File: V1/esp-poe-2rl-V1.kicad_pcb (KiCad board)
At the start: 2 copper layers, 89 x 45 mm, 90 parts, among them J1 USB_C_Receptacle_USB2.0, J2 RJ45 JACK, J3 1x2P 5,08mm, J4 1x2P 5,08mm, K1 G5NB-1A-E-DC5, K2 G5NB-1A-E-DC5, Q1 UMH3N, Q2 WPM2015-3/TR, Q3 LMUN2211LT1G, Q4 MMBT2222A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

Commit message: Update image
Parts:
- J3, J4: footprint Tales:TerminalBlock_Dibo_DB142R-2-5.08_1x02_P5.08mm_Horizontal -> Tales:TerminalBlock_Dibo_DB142R-5.08-2P_1x02_P5.08mm_Horizontal
- L2: footprint Tales:L_3x3_h1.5 -> Tales:L_3x3mm_h1.5mm

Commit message: Added temperature sensor
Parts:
- added C26: 100nF/50V, Tales:C_0402_1005Metric, F.Cu at (124.4, 60.1)
- added R31: 2k2/62,5mW, Tales:R_0402_1005Metric, F.Cu at (121.5, 60.1)
- added R32: 2k2/62,5mW, Tales:R_0402_1005Metric, F.Cu at (121.5, 62.1)
- added U7: AHT20, Tales:DFN-6-3x3mm_P1mm, F.Cu at (117.4, 61.5)
- D10, D9: footprint Tales:D_SOD-123 -> Diode_THT:D_DO-35_SOD27_P7.62mm_Horizontal
- Q1: footprint Tales:SOT-363_SC-70-6 -> Package_TO_SOT_SMD:SOT-363_SC-70-6
- U2: footprint Tales:SOIC-8-1EP_3.9x4.9mm_P1.27mm_EP2.29x3mm_ThermalVias -> Tales:SOIC-8-1EP_3.9x4.9mm_P1.27mm_EP2.41x3.81mm_ThermalVias
- U4: footprint Tales:SOIC-16_3.9x9.9mm_P1.27mm -> Package_SO:SOIC-16_3.9x9.9mm_P1.27mm
- U5: footprint Tales:ESP32-WROOM-32U -> RF_Module:ESP32-WROOM-32U
- U6: footprint Tales:QFN-32-1EP_5x5mm_P0.5mm_EP3.3x3.3mm_ThermalVias -> Package_DFN_QFN:QFN-32-1EP_5x5mm_P0.5mm_EP3.3x3.3mm_ThermalVias
- moved K1 0.23 mm to (83.8, 80.6)
- moved K2 0.21 mm to (97.2, 80.6)
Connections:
- U5 pad 16: unconnected-(U5-IO13-Pad16) -> OUT1
- U5 pad 27: unconnected-(U5-IO16-Pad27) -> OUT2
- U5 pad 8: OUT2 -> I2C_SCL
- U5 pad 9: OUT1 -> I2C_SDA
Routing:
- net OUT1: track 20.0 -> 1.50 mm
- net OUT2: track 8.27 -> 1.50 mm

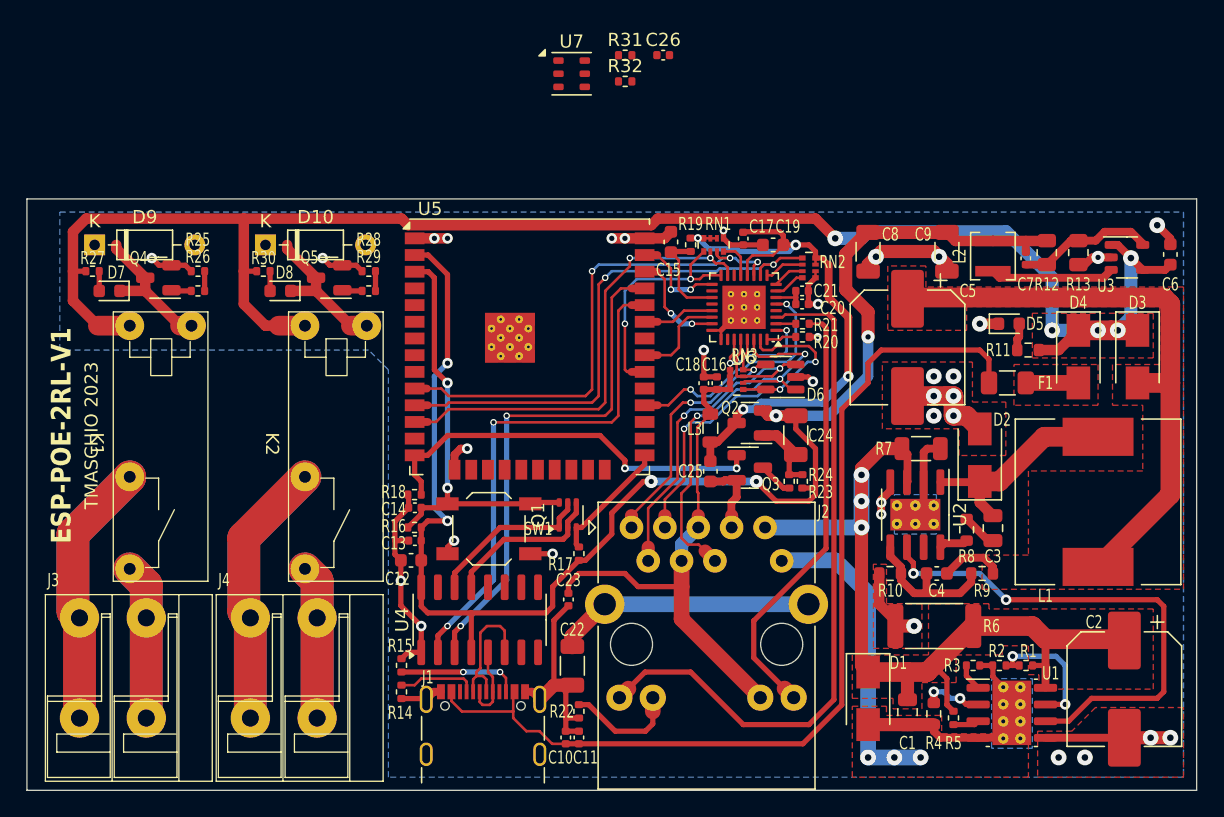
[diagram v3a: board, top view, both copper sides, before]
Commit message: Added temperature sensor.
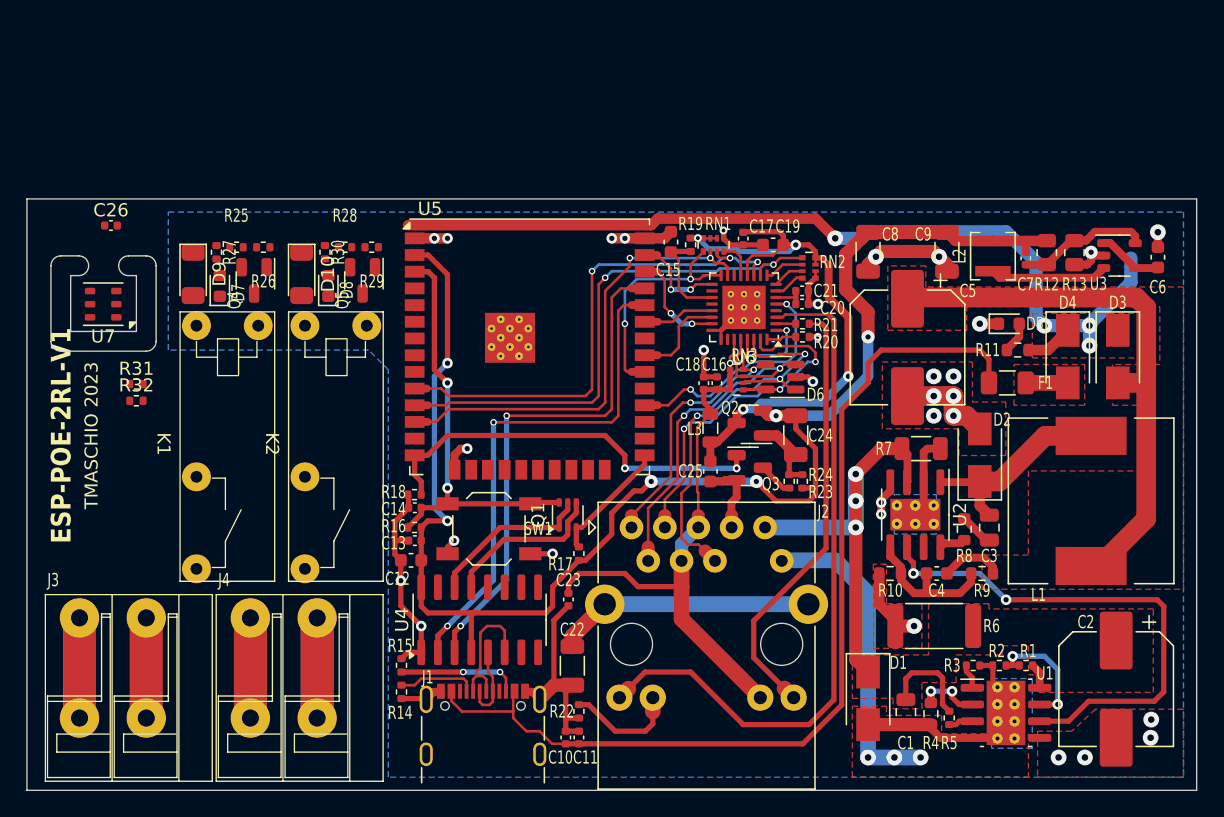
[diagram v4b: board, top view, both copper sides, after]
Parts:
- D10, D9: footprint Diode_THT:D_DO-35_SOD27_P7.62mm_Horizontal -> Tales:D_SOD-123
- moved R31 44.8 mm to (84.3, 85.1)
- moved R32 44.4 mm to (84.3, 86.4)
- moved C26 44.0 mm to (82.4, 73.0)
- moved U7 39.7 mm to (81.8, 79.0), turned to 180 degrees
- moved R27 9.54 mm to (90.4, 75.1), turned to -90 degrees
- moved D7 8.40 mm to (90.7, 77.6), turned to 90 degrees
- moved D9 7.81 mm to (88.6, 76.7), turned to -90 degrees
- moved Q4 7.29 mm to (93.3, 77.2), turned to -90 degrees
- moved R26 5.98 mm to (94.0, 74.7), turned to 180 degrees
- moved K1 5.08 mm to (88.9, 80.6)
- moved R30 4.91 mm to (98.7, 75.1), turned to -90 degrees
- moved D8 3.66 mm to (98.9, 77.6), turned to 90 degrees
- moved D10 3.53 mm to (96.9, 76.7), turned to -90 degrees
- moved R25 3.46 mm to (92.0, 74.7)
- moved R29 3.33 mm to (102.2, 74.7), turned to 180 degrees
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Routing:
- net +5V: track 130.2 -> 74.8 mm, vias 5 -> 4
- net Net-(J4-Pin_1): track 41.0 -> 15.2 mm
- net Net-(J3-Pin_1): track 40.7 -> 15.2 mm
- net PoE+: track 65.6 -> 42.9 mm
- net GND: track 113.2 -> 97.1 mm, vias 34 -> 32
- net Net-(D10-A): track 11.3 -> 0.00 mm
- net Net-(D7-K): track 11.0 -> 0.00 mm
- net Net-(J3-Pin_2): track 23.8 -> 15.2 mm
- net Net-(J4-Pin_2): track 23.5 -> 15.2 mm
- net 5VPOE: track 49.7 -> 47.1 mm
- net OUT2: track 1.50 -> 0.00 mm
- net OUT1: track 1.50 -> 0.00 mm
- net Net-(D8-A): track 1.50 -> 0.00 mm
- net Net-(D7-A): track 1.50 -> 0.00 mm
- net Net-(Q5-B): track 1.45 -> 0.00 mm
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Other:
- outline, holes or cut-outs redrawn

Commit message: Reviewing board for fabrication
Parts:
- U3: footprint Tales:TSOT-23-5 -> Tales:SOT-23-5_Shorter_Pins
- U5: footprint RF_Module:ESP32-WROOM-32U -> Tales:ESP32-WROOM-32U
- U6: footprint Package_DFN_QFN:QFN-32-1EP_5x5mm_P0.5mm_EP3.3x3.3mm_ThermalVias -> Tales:QFN-32-1EP_5x5mm_P0.5mm_EP3.3x3.3mm_ThermalVias
- moved RN1 0.21 mm to (128.3, 74.3)
- moved C19 0.20 mm to (132.8, 74.3)
- moved C20 0.15 mm to (135.1, 79.0)
- moved C21 0.15 mm to (135.1, 78.0)
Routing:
- net +5V: track 74.8 -> 113.5 mm, vias 4 -> 5
- net GND: track 97.1 -> 103.3 mm, vias 32 -> 34
- net Net-(D7-K): track 0.00 -> 5.27 mm
- net Net-(D10-A): track 0.00 -> 5.27 mm
- net +3.3VLAN: track 46.6 -> 49.5 mm
- net Net-(Q4-B): track 0.00 -> 1.63 mm
- net Net-(Q5-B): track 0.00 -> 1.63 mm
- net Net-(U4-RXD): track 39.1 -> 37.7 mm
- net Net-(D8-A): track 0.00 -> 1.38 mm
- net Net-(D7-A): track 0.00 -> 1.37 mm
- net /EMAC_MDC: track 7.32 -> 8.59 mm
- net OUT1: track 0.00 -> 1.01 mm
- net OUT2: track 0.00 -> 1.01 mm
- net /EMAC_MDIO: track 17.9 -> 18.7 mm
- net /EMAC_CLK: track 18.4 -> 17.6 mm
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
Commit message: Update esp-poe-2rl-V1.kicad_pcb
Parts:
- moved C7 1.55 mm to (151.6, 74.0)
- moved U3 0.83 mm to (159.2, 74.5)
- moved R13 0.82 mm to (155.2, 74.4), turned to 90 degrees
- moved L2 0.78 mm to (149.1, 74.7)
- moved R12 0.78 mm to (153.2, 74.4)
- moved C6 0.24 mm to (162.1, 75.2)
- moved C8 0.08 mm to (140.1, 75.0)
- moved C9 0.08 mm to (145.9, 75.0)
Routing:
- net 5VPOE: track 47.1 -> 5.39 mm
- net Net-(J3-Pin_1): track 15.2 -> 48.6 mm
- net Net-(J4-Pin_1): track 15.2 -> 42.5 mm
- net +3.3V: track 117.1 -> 93.2 mm
- net Net-(J3-Pin_2): track 15.2 -> 28.2 mm
- net GND: track 103.3 -> 90.9 mm, vias 34 -> 33
- net Net-(U3-FB): track 9.93 -> 0.00 mm
- net Net-(U3-LX): track 8.94 -> 0.00 mm
- net Net-(J4-Pin_2): track 15.2 -> 23.5 mm
- net +5V: track 113.5 -> 107.1 mm, vias 5 -> 4
- net /TD-: track 29.2 -> 25.8 mm
- net Net-(D10-A): track 5.27 -> 7.32 mm
- net Net-(D7-K): track 5.27 -> 7.32 mm
- net Net-(U4-TXD): track 38.6 -> 37.5 mm
- removed copper zone on B.Cu, net GND

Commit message: Update esp-poe-2rl-V1.kicad_pcb
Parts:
- moved C6 0.55 mm to (161.5, 75.2)
- moved U3 0.49 mm to (158.7, 74.5)
- moved C4 0.25 mm to (145.5, 99.5)
- moved R4 0.22 mm to (145.0, 110.2)
- moved L2 0.16 mm to (149.2, 74.7)
- moved C1 0.12 mm to (143.0, 110.0)
- moved C7 0.12 mm to (151.8, 74.0)
- moved C8 0.10 mm to (140.0, 75.0)
- moved R12 0.09 mm to (153.2, 74.4)
- moved U1 0.08 mm to (150.6, 110.2)
- moved C9 0.08 mm to (146.0, 75.0)
- moved L1 0.08 mm to (157.0, 94.0)
- moved R5 0.07 mm to (146.2, 110.5)
- moved R13 0.07 mm to (155.2, 74.4)
- moved D4 0.06 mm to (155.2, 83.0)
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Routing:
- net PoE+: track 42.9 -> 12.2 mm
- net GND: track 90.9 -> 73.8 mm, vias 33 -> 31
- net Net-(D2-K): track 15.7 -> 0.00 mm
- net Net-(C10-Pad1): track 73.0 -> 58.3 mm
- net PoE-: track 37.3 -> 24.2 mm
- net Net-(U2-FB): track 11.3 -> 0.00 mm
- net 5VPOE: track 5.39 -> 0.00 mm
- net Net-(R7-Pad2): track 5.35 -> 0.00 mm
- net PG: track 38.0 -> 33.4 mm
- net 5VUSB: track 3.19 -> 0.00 mm
- net Net-(U1-CLASS): track 4.90 -> 2.04 mm
- net Net-(U1-UVLO): track 9.13 -> 6.50 mm
- net Net-(D5-A): track 2.39 -> 0.00 mm
- net Net-(C3-Pad1): track 2.53 -> 0.14 mm
- net +5V: track 107.1 -> 105.0 mm
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- removed copper zone on F.Cu, net 5VUSB

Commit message: Update esp-poe-2rl-V1.kicad_pcb
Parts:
- moved C26 7.73 mm to (81.8, 80.7), turned to -90 degrees
- moved U7 2.76 mm to (81.8, 76.2)
- moved R31 2.57 mm to (83.3, 82.8)
- moved R32 2.37 mm to (83.3, 84.2)
- moved R11 0.71 mm to (151.9, 82.0)
- moved C4 0.50 mm to (145.5, 100.0)
- moved R10 0.50 mm to (141.7, 100.0)
- moved R9 0.50 mm to (148.7, 100.0)
- moved D5 0.25 mm to (150.5, 80.5)
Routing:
- net +3.3V: track 93.2 -> 152.0 mm, vias 6 -> 8
- net I2C_SDA: track 0.00 -> 36.1 mm
- net OUT1: track 1.01 -> 34.9 mm, vias 0 -> 2
- net OUT2: track 1.01 -> 33.1 mm, vias 0 -> 2
- net I2C_SCL: track 0.00 -> 31.0 mm
- net PoE+: track 12.2 -> 42.7 mm
- net GND: track 73.8 -> 93.2 mm, vias 31 -> 34
- net Net-(D2-K): track 0.00 -> 15.8 mm
- net +5V: track 105.0 -> 120.3 mm
- net Net-(C10-Pad1): track 58.3 -> 72.3 mm
- net Net-(U3-FB): track 0.00 -> 12.5 mm, vias 0 -> 2
- net Net-(U2-FB): track 0.00 -> 9.85 mm
- net Net-(U3-LX): track 0.00 -> 9.00 mm
- net Net-(R7-Pad2): track 0.00 -> 6.46 mm
- net PG: track 33.4 -> 38.5 mm
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- added copper zone on B.Cu, net GND
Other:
- outline, holes or cut-outs redrawn
- board text added: "TMASCHIO 2024"
- board text removed: "TMASCHIO 2023"
